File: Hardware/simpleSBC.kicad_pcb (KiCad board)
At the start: 6 copper layers, 49 x 55 mm, 124 parts, among them J1 Conn_02x07_Odd_Even, J2 Micro_SD_Card_Det, J3 Conn_01x06_Male, U1 STM32MP157FAD1, U2 LP2998, U3 MT41K256M16TW, X1 ASCO, Y1 32.786

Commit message: First Draft schematic (R2)
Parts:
- removed C39, C43, C44: 100u, Capacitor_SMD:C_1206_3216Metric
- removed C41: 4.7u, Capacitor_SMD:C_0402_1005Metric
- removed C42: 1u, Capacitor_SMD:C_0402_1005Metric
- removed C47: 100n, Capacitor_SMD:C_0402_1005Metric
- removed TP7, TP9: TestPoint, personal:PROBE_PAD_1206
- removed U2: LP2998, Package_SO:SOIC-8-1EP_3.9x4.9mm_P1.27mm_EP2.29x3mm_ThermalVias
- added C67: 1u, Capacitor_SMD:C_0402_1005Metric, F.Cu at (108.4, 42.9)
- added C68: 1u, Capacitor_SMD:C_0402_1005Metric, F.Cu at (108.4, 44.9)
- added C69: 1u, Capacitor_SMD:C_0402_1005Metric, F.Cu at (108.4, 46.9)
- added C70: 10u, Capacitor_SMD:C_0402_1005Metric, F.Cu at (108.4, 48.8)
- added C71: 10u, Capacitor_SMD:C_0402_1005Metric, F.Cu at (108.4, 50.8)
- added C72: 10u, Capacitor_SMD:C_0402_1005Metric, F.Cu at (111.3, 42.9)
- added C73: 10u, Capacitor_SMD:C_0402_1005Metric, F.Cu at (111.3, 44.9)
- added C74: 4.7u, Capacitor_SMD:C_0402_1005Metric, F.Cu at (111.3, 46.9)
- added C75: 1u, Capacitor_SMD:C_0402_1005Metric, F.Cu at (111.3, 48.8)
- added C76: 1u, Capacitor_SMD:C_0402_1005Metric, F.Cu at (111.3, 50.8)
- added J5: USB_A, Connector_USB:USB_A_Molex_67643_Horizontal, F.Cu at (147.8, 70.9)
- added J6: USB_A, Connector_USB:USB_A_Molex_67643_Horizontal, F.Cu at (127.0, 70.9)
- added U4: STPMIC1, SimpleSBC:WFQFN44L, F.Cu at (119.8, 103.0)
- U1: footprint personal:TFBGA257 -> SimpleSBC:TFBGA257
- moved TP6 41.8 mm to (134.5, 32.2)
- moved TP2 28.6 mm to (152.1, 48.2)
- moved TP4 26.1 mm to (127.0, 44.0)
- moved TP1 16.0 mm to (141.0, 47.2)
- moved TP5 15.9 mm to (120.5, 46.8)
- moved TP3 15.6 mm to (133.0, 47.8)
- moved TP8 13.4 mm to (166.0, 95.5)
- moved J2 13.3 mm to (139.8, 107.0), turned to 180 degrees
- moved R11 11.2 mm to (142.2, 98.7)
- moved R12 11.2 mm to (134.4, 98.7)
- moved R14 11.2 mm to (136.8, 98.7)
- moved R15 11.2 mm to (138.8, 98.7)
- moved R10 11.2 mm to (141.0, 98.7)
- moved R13 11.2 mm to (135.6, 98.7)
- moved J1 10.2 mm to (148.2, 107.6), turned to 90 degrees
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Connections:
- net /A0 renamed /Memory/A0
- net /A1 renamed /Memory/A1
- net /A10 renamed /Memory/A10
- net /A11 renamed /Memory/A11
- net /A12 renamed /Memory/A12
- net /A13 renamed /Memory/A13
- net /A14 renamed /Memory/A14
- net /A2 renamed /Memory/A2
- net /A3 renamed /Memory/A3
- net /A4 renamed /Memory/A4
- net /A5 renamed /Memory/A5
- net /A6 renamed /Memory/A6
- net /A7 renamed /Memory/A7
- net /A8 renamed /Memory/A8
- net /A9 renamed /Memory/A9
- net /BA0 renamed /Memory/BA0
- net /BA1 renamed /Memory/BA1
- net /BA2 renamed /Memory/BA2
- net /CKE renamed /Memory/CKE
- net /DDR_CK+ renamed /Memory/DDR_CK+
- net /DDR_CK- renamed /Memory/DDR_CK-
- net /DQ0 renamed /Memory/DQ0
- net /DQ1 renamed /Memory/DQ1
- net /DQ10 renamed /Memory/DQ10
- net /DQ11 renamed /Memory/DQ11
- net /DQ12 renamed /Memory/DQ12
- net /DQ13 renamed /Memory/DQ13
- net /DQ14 renamed /Memory/DQ14
- net /DQ15 renamed /Memory/DQ15
- net /DQ2 renamed /Memory/DQ2
- net /DQ3 renamed /Memory/DQ3
- net /DQ4 renamed /Memory/DQ4
- net /DQ5 renamed /Memory/DQ5
- net /DQ6 renamed /Memory/DQ6
- net /DQ7 renamed /Memory/DQ7
- net /DQ8 renamed /Memory/DQ8
- net /DQ9 renamed /Memory/DQ9
- net /LDM renamed /Memory/LDM
- net /LDQS+ renamed /Memory/LDQS+
- net /LDQS- renamed /Memory/LDQS-
- net /ODT renamed /Memory/ODT
- net /UDM renamed /Memory/UDM
- net /UDQS+ renamed /Memory/UDQS+
- net /UDQS- renamed /Memory/UDQS-
- net /~{CAS} renamed /Memory/~{CAS}
- net /~{CS} renamed /Memory/~{CS}
- net /~{RAS} renamed /Memory/~{RAS}
- net /~{RESET} renamed /Memory/~{RESET}
- net /~{WE} renamed /Memory/~{WE}
- J2 pad 1: /SDMMC_D2 -> /Memory/SDMMC_D2
- J2 pad 2: /SDMMC_D3 -> /Memory/SDMMC_D3
- J2 pad 3: /SDMMC_CMD -> /Memory/SDMMC_CMD
- J2 pad 5: /SDMMC_CLK -> /Memory/SDMMC_CLK
- J2 pad 7: /SDMMC_D0 -> /Memory/SDMMC_D0
- J2 pad 8: /SDMMC_D1 -> /Memory/SDMMC_D1
- R10 pad 1: /SDMMC_D0 -> /Memory/SDMMC_D0
- R11 pad 1: /SDMMC_D1 -> /Memory/SDMMC_D1
- R12 pad 1: /SDMMC_D2 -> /Memory/SDMMC_D2
- R13 pad 1: /SDMMC_D3 -> /Memory/SDMMC_D3
- R14 pad 1: /SDMMC_CMD -> /Memory/SDMMC_CMD
- R15 pad 1: /SDMMC_CLK -> /Memory/SDMMC_CLK
- U1 pad N3: unconnected-(U1-PadN3) -> /PA0_WAKEUP
- U1 pad V10: unconnected-(U1-PadV10) -> Net-(J5-D+)
- U1 pad V14: unconnected-(U1-PadV14) -> Net-(J6-D-)
- U1 pad W10: unconnected-(U1-PadW10) -> Net-(J5-D-)
- U1 pad W14: unconnected-(U1-PadW14) -> Net-(J6-D+)
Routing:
- net /SDMMC_D2: track 30.6 -> 0.00 mm, vias 2 -> 0
- net /Memory/SDMMC_D2: track 0.00 -> 30.6 mm, vias 0 -> 2
- net /SDMMC_CMD: track 30.0 -> 0.00 mm, vias 2 -> 0
- net /Memory/SDMMC_CMD: track 0.00 -> 30.0 mm, vias 0 -> 2
- net /SDMMC_CLK: track 29.1 -> 0.00 mm, vias 2 -> 0
- net /Memory/SDMMC_CLK: track 0.00 -> 29.1 mm, vias 0 -> 2
- net /SDMMC_D0: track 26.2 -> 0.00 mm, vias 2 -> 0
- net /Memory/SDMMC_D0: track 0.00 -> 26.2 mm, vias 0 -> 2
- net /IO2: track 13.2 -> 0.00 mm
- net /IO6: track 13.2 -> 0.00 mm
- net /IO3: track 12.4 -> 0.00 mm
- net /IO5: track 12.3 -> 0.00 mm
- net /IO4: track 11.9 -> 0.00 mm
- net /IO1: track 14.5 -> 3.30 mm
- net VTT_DDR: track 18.2 -> 9.38 mm, vias 7 -> 3
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- removed copper zone on F.Cu, net +1V2
- removed copper zone on F.Cu, net +1V35
- removed copper zone on F.Cu, net +3V3
- removed copper zone on F.Cu, net VTT_DDR
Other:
- outline, holes or cut-outs redrawn
- board text added: "Hans Gaensbauer and Tim Shepard"
- board text added: "SimpleSBC"
- board text removed: "Ap-Eval Designed by Hans Gaensbauer"

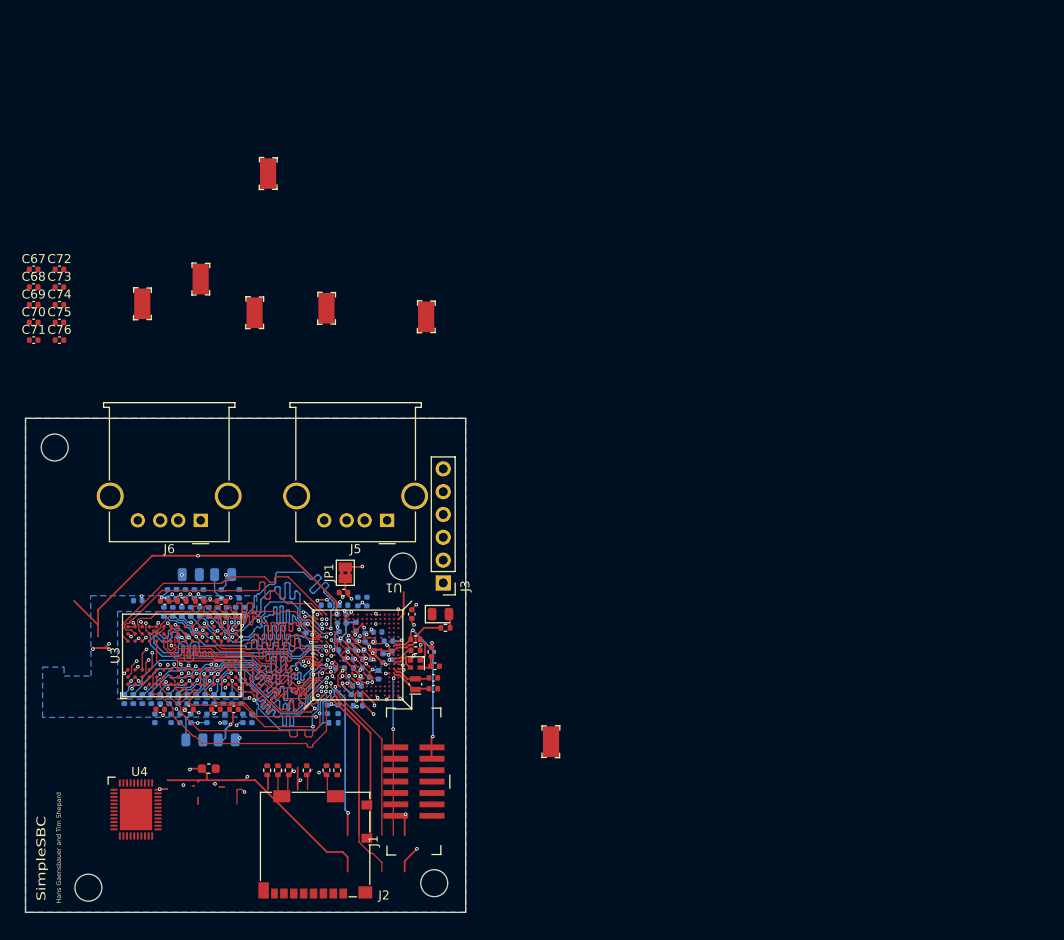
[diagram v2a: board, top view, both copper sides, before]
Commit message: Add Ethernet and USB power switching
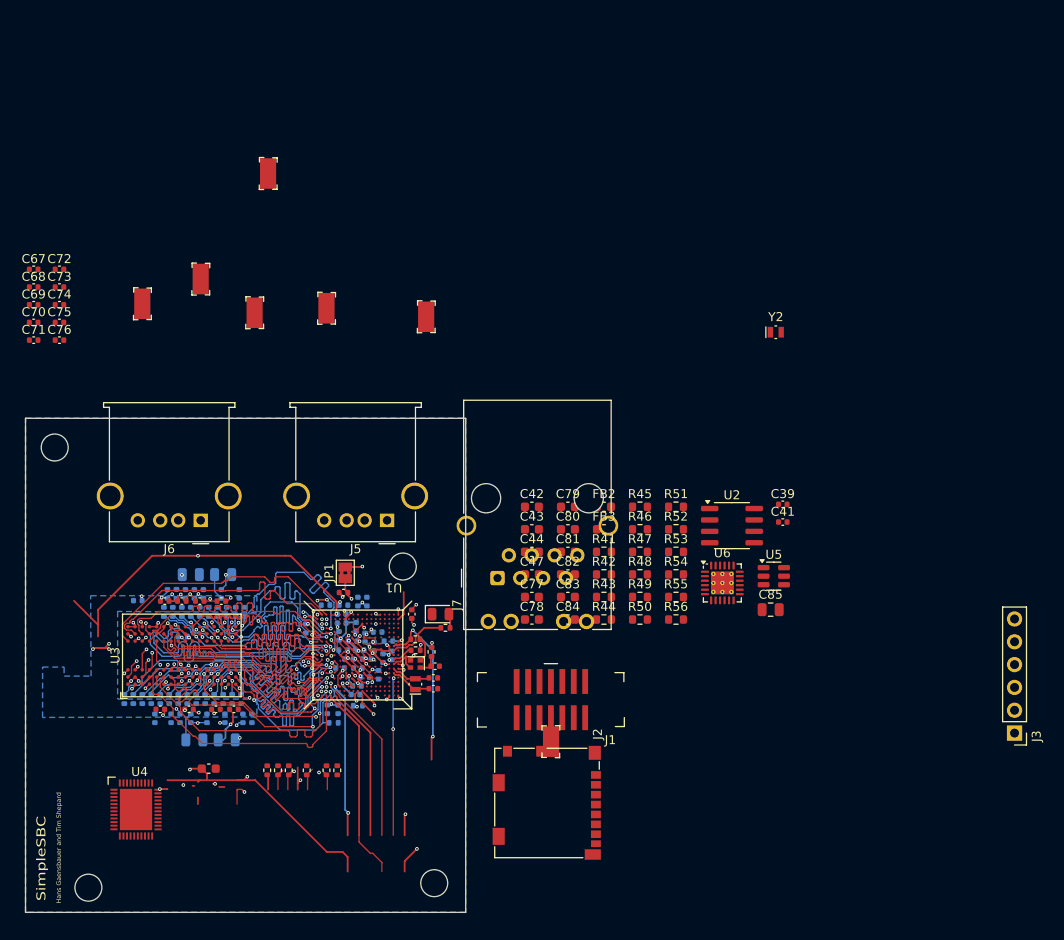
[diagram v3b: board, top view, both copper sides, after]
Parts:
- added C39: 47u, Capacitor_SMD:C_0402_1005Metric, F.Cu at (191.8, 69.1)
- added C41: 47u, Capacitor_SMD:C_0402_1005Metric, F.Cu at (191.8, 71.0)
- added C42: 30p, Capacitor_SMD:C_0603_1608Metric, F.Cu at (163.9, 69.3)
- added C43: 100n, Capacitor_SMD:C_0603_1608Metric, F.Cu at (163.9, 71.9)
- added C44: 30p, Capacitor_SMD:C_0603_1608Metric, F.Cu at (163.9, 74.4)
- added C47: 100n, Capacitor_SMD:C_0603_1608Metric, F.Cu at (163.9, 76.9)
- added C77: 1u, Capacitor_SMD:C_0603_1608Metric, F.Cu at (163.9, 79.4)
- added C78: 1u, Capacitor_SMD:C_0603_1608Metric, F.Cu at (163.9, 81.9)
- added C79: 1u, Capacitor_SMD:C_0603_1608Metric, F.Cu at (167.9, 69.3)
- added C80: 470p, Capacitor_SMD:C_0603_1608Metric, F.Cu at (167.9, 71.9)
- added C81: 100n, Capacitor_SMD:C_0603_1608Metric, F.Cu at (167.9, 74.4)
- added C82: 100n, Capacitor_SMD:C_0603_1608Metric, F.Cu at (167.9, 76.9)
- added C83: 100n, Capacitor_SMD:C_0603_1608Metric, F.Cu at (167.9, 79.4)
- added C84: 100n, Capacitor_SMD:C_0603_1608Metric, F.Cu at (167.9, 81.9)
- added C85: 10u, Capacitor_SMD:C_0805_2012Metric, F.Cu at (190.4, 80.8)
- added FB2: FerriteBead_Small, Inductor_SMD:L_0603_1608Metric, F.Cu at (171.9, 69.3)
- added FB3: FerriteBead_Small, Inductor_SMD:L_0603_1608Metric, F.Cu at (171.9, 71.9)
- added J7: RJ45_Wuerth_7499010121A, Connector_RJ:RJ45_Wuerth_7499010121A_Horizontal, F.Cu at (160.0, 77.3)
- added R41: 10k, Resistor_SMD:R_0603_1608Metric, F.Cu at (171.9, 74.4)
- added R42: 33, Resistor_SMD:R_0603_1608Metric, F.Cu at (171.9, 76.9)
- added R43: 33, Resistor_SMD:R_0603_1608Metric, F.Cu at (171.9, 79.4)
- added R44: 33, Resistor_SMD:R_0603_1608Metric, F.Cu at (171.9, 81.9)
- added R45: 270, Resistor_SMD:R_0603_1608Metric, F.Cu at (175.9, 69.3)
- added R46: 10k, Resistor_SMD:R_0603_1608Metric, F.Cu at (175.9, 71.9)
- added R47: 10k, Resistor_SMD:R_0603_1608Metric, F.Cu at (175.9, 74.4)
- added R48: 33, Resistor_SMD:R_0603_1608Metric, F.Cu at (175.9, 76.9)
- added R49: 10k, Resistor_SMD:R_0603_1608Metric, F.Cu at (175.9, 79.4)
- added R50: 270, Resistor_SMD:R_0603_1608Metric, F.Cu at (175.9, 81.9)
- added R51: 10k, Resistor_SMD:R_0603_1608Metric, F.Cu at (179.9, 69.3)
- added R52: 51, Resistor_SMD:R_0603_1608Metric, F.Cu at (179.9, 71.9)
- added R53: 51, Resistor_SMD:R_0603_1608Metric, F.Cu at (179.9, 74.4)
- added R54: 12.1k, Resistor_SMD:R_0603_1608Metric, F.Cu at (179.9, 76.9)
- added R55: 51, Resistor_SMD:R_0603_1608Metric, F.Cu at (179.9, 79.4)
- added R56: 51, Resistor_SMD:R_0603_1608Metric, F.Cu at (179.9, 81.9)
- added U2: STMPS2252MTR, Package_SO:SOIC-8_3.9x4.9mm_P1.27mm, F.Cu at (186.1, 71.5)
- added U5: USBLC6-4SC6, Package_TO_SOT_SMD:SOT-23-6, F.Cu at (190.8, 77.1)
- added U6: LAN8742A, Package_DFN_QFN:VQFN-24-1EP_4x4mm_P0.5mm_EP2.5x2.5mm_ThermalVias, F.Cu at (185.1, 77.8)
- added Y2: X53T-C20SSA-25.000MHz, Crystal:Crystal_SMD_MicroCrystal_CM9V-T1A-2Pin_1.6x1.0mm, F.Cu at (191.0, 49.9)
- moved J3 65.8 mm to (217.6, 94.5)
- moved J1 29.1 mm to (173.6, 93.3), turned to 180 degrees
- moved J2 26.2 mm to (165.6, 102.3), turned to -90 degrees
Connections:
- J5 pad 1: unconnected-(J5-VBUS-Pad1) -> Net-(J5-VBUS)
- J6 pad 1: unconnected-(J6-VBUS-Pad1) -> Net-(J6-VBUS)
- U1 pad R2: unconnected-(U1B-PG14-PadR2) -> /RMII_TXD_1
- U1 pad R3: unconnected-(U1B-PG13-PadR3) -> /RMII_TXD_0
- U1 pad T1: unconnected-(U1B-PA1-PadT1) -> /RMII_REF_CLK
- U1 pad T2: unconnected-(U1B-PC1-PadT2) -> /MDC
- U1 pad T3: unconnected-(U1B-PA2-PadT3) -> /MDIO
- U1 pad U3: unconnected-(U1B-PB11-PadU3) -> /RMII_TX_EN
- U1 pad V1: /IO1 -> /RMII_RX_D1
- U1 pad V2: unconnected-(U1B-PC4-PadV2) -> /RMII_RX_D0
- U1 pad W2: /IO2 -> /RMII_CRS_DV
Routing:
- net /RMII_RX_D1: track 0.00 -> 3.30 mm
- net /IO1: track 3.30 -> 0.00 mm

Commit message: First pass through ST Design Checklist
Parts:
- removed J3: Conn_01x06_Male, Connector_PinHeader_2.54mm:PinHeader_1x06_P2.54mm_Vertical
- added C86: 4.7u, Capacitor_SMD:C_0402_1005Metric, F.Cu at (180.7, 33.2)
- added FB1: FerriteBead_Small, Inductor_SMD:L_0603_1608Metric, F.Cu at (164.1, 37.9)
- added J4: Barrel_Jack_Switch, Connector_BarrelJack:BarrelJack_Wuerth_6941xx301002, F.Cu at (167.6, 18.5)
- added J8: Conn_01x03, Connector_PinHeader_2.54mm:PinHeader_1x03_P2.54mm_Vertical, F.Cu at (181.6, 18.9)
- added J9: Conn_01x06, Connector_PinHeader_2.54mm:PinHeader_1x06_P2.54mm_Vertical, F.Cu at (206.6, 74.1)
- added L1: 1u, Inductor_SMD:L_1008_2520Metric, F.Cu at (176.8, 18.4)
- added L2: 1u, Inductor_SMD:L_1008_2520Metric, F.Cu at (176.8, 22.2)
- added L3: 1u, Inductor_SMD:L_1008_2520Metric, F.Cu at (176.8, 25.9)
- added L4: 1u, Inductor_SMD:L_1008_2520Metric, F.Cu at (176.8, 29.7)
- added R57: 2.2k, Resistor_SMD:R_0402_1005Metric, F.Cu at (180.7, 29.2)
- added R58: 2.2k, Resistor_SMD:R_0402_1005Metric, F.Cu at (180.7, 31.2)
- added R9: 0, Resistor_SMD:R_0402_1005Metric, F.Cu at (180.7, 27.2)
- added TP10: TestPoint, TestPoint:TestPoint_Pad_D1.0mm, F.Cu at (175.9, 33.1)
- C42, C43, C44, C47, C77, C78, C79, C80, C81, C82, C83, C84: footprint Capacitor_SMD:C_0603_1608Metric -> Capacitor_SMD:C_0402_1005Metric
- J1: footprint personal:PinHeader_2x7_P1.27mm_SMD -> SimpleSBC:PinHeader_2x7_P1.27mm_SMD
- J2: value Micro_SD_Card_Det -> Micro_SD_Card_Det2
- R41, R42, R43, R44, R45, R46, R47, R48, R49, R50, R51, R52, R53, R54, R55, R56: footprint Resistor_SMD:R_0603_1608Metric -> Resistor_SMD:R_0402_1005Metric
- TP1, TP2, TP3, TP4, TP5, TP6: value TestPoint-SP -> TestPoint; footprint personal:PROBE_PAD_1206 -> TestPoint:TestPoint_Pad_D1.0mm
- TP8: footprint personal:PROBE_PAD_1206 -> TestPoint:TestPoint_Pad_D1.0mm
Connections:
- J2 pad 1: /Memory/SDMMC_D2 -> /SDMMC_D2
- J2 pad 2: /Memory/SDMMC_D3 -> /SDMMC_D3
- J2 pad 3: /Memory/SDMMC_CMD -> /SDMMC_CMD
- J2 pad 5: /Memory/SDMMC_CLK -> /SDMMC_CLK
- J2 pad 7: /Memory/SDMMC_D0 -> /SDMMC_D0
- J2 pad 8: /Memory/SDMMC_D1 -> /SDMMC_D1
- R10 pad 1: /Memory/SDMMC_D0 -> /SDMMC_D0
- R11 pad 1: /Memory/SDMMC_D1 -> /SDMMC_D1
- R12 pad 1: /Memory/SDMMC_D2 -> /SDMMC_D2
- R13 pad 1: /Memory/SDMMC_D3 -> /SDMMC_D3
- R14 pad 1: /Memory/SDMMC_CMD -> /SDMMC_CMD
- R15 pad 1: /Memory/SDMMC_CLK -> /SDMMC_CLK
- TP1 pad 1: +3V3 -> +1V2
- TP2 pad 1: GND -> +1V35
- TP3 pad 1: +1V2 -> +3V3
- TP4 pad 1: GND -> +3.3VP
- TP5 pad 1: +1V35 -> VREF_DDR
- TP6 pad 1: GND -> VTT_DDR
- U4 pad 20: unconnected-(U4-LDO5OUT-Pad20) -> Net-(U4-LDO5OUT)
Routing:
- net (no net): track 0.00 -> 79.8 mm
- net /Memory/SDMMC_D2: track 30.6 -> 0.00 mm, vias 2 -> 0
- net /Memory/SDMMC_CMD: track 30.0 -> 0.00 mm, vias 2 -> 0
- net /SDMMC_CMD: track 0.00 -> 29.8 mm, vias 0 -> 2
- net /Memory/SDMMC_CLK: track 29.1 -> 0.00 mm, vias 2 -> 0
- net /Memory/SDMMC_D0: track 26.2 -> 0.00 mm, vias 2 -> 0
- net /SDMMC_CLK: track 0.00 -> 2.55 mm, vias 0 -> 2
- net /Memory/SDMMC_D3: track 2.33 -> 0.00 mm
- net /SDMMC_D3: track 28.9 -> 31.3 mm
- net /SDMMC_D0: track 0.00 -> 2.06 mm, vias 0 -> 2
- net /SDMMC_D2: track 0.00 -> 1.68 mm, vias 0 -> 2

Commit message: First Pass for Floorplanning
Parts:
- removed C45: 1u, Capacitor_SMD:C_0402_1005Metric
- removed FB2: FerriteBead_Small, Inductor_SMD:L_0603_1608Metric
- removed Y2: X53T-C20SSA-25.000MHz, Crystal:Crystal_SMD_MicroCrystal_CM9V-T1A-2Pin_1.6x1.0mm
- added C87: 10u, Capacitor_SMD:C_0603_1608Metric, F.Cu at (127.2, 111.5)
- added C88: 4.7u, Capacitor_SMD:C_0402_1005Metric, F.Cu at (132.2, 99.0)
- added C89: 10u, Capacitor_SMD:C_0603_1608Metric, F.Cu at (136.9, 98.0)
- added C90: 22u, Capacitor_SMD:C_0805_2012Metric, F.Cu at (124.9, 101.8)
- added C91: 22u, Capacitor_SMD:C_0805_2012Metric, F.Cu at (123.7, 106.5)
- added C92: 22u, Capacitor_SMD:C_0805_2012Metric, F.Cu at (140.8, 104.2)
- added C93: 22u, Capacitor_SMD:C_0805_2012Metric, F.Cu at (139.2, 108.8)
- added C94: 10u, Capacitor_SMD:C_0603_1608Metric, F.Cu at (128.7, 111.5)
- added C95: 4.7u, Capacitor_SMD:C_0402_1005Metric, F.Cu at (133.9, 111.0)
- added C96: 4.7u, Capacitor_SMD:C_0402_1005Metric, F.Cu at (134.9, 108.0)
- added C97: 10n, Capacitor_SMD:C_0402_1005Metric, F.Cu at (166.5, 107.2)
- added D2: LED_Small, LED_SMD:LED_0805_2012Metric, F.Cu at (153.8, 78.5)
- added R59: 0, Resistor_SMD:R_0402_1005Metric, F.Cu at (135.9, 99.8)
- added R60: 10k, Resistor_SMD:R_0402_1005Metric, F.Cu at (157.2, 107.2)
- added R61: 330, Resistor_SMD:R_0402_1005Metric, F.Cu at (154.2, 77.0)
- added R62: 3k, Resistor_SMD:R_0402_1005Metric, F.Cu at (146.0, 78.2)
- added R63: 10k, Resistor_SMD:R_0402_1005Metric, F.Cu at (167.5, 107.2)
- C40: value 100n -> 10n
- C51, C77, C78, C81, C82, R10, R11, R12, R13, R14, R15, R45, R47, R50, TP1, TP10, TP2, TP3, TP4, TP5, TP6: moved to B.Cu
- C69, C76: value 1u -> 4.7u
- C70, C71, C72, C73: footprint Capacitor_SMD:C_0402_1005Metric -> Capacitor_SMD:C_0603_1608Metric
- R8: value 1k -> 470
- moved J8 103.7 mm to (110.5, 94.3), turned to 180 degrees
- moved J4 98.2 mm to (113.4, 100.4)
- moved L2 98.2 mm to (126.9, 106.8), turned to 180 degrees
- moved L1 97.1 mm to (127.4, 102.0), turned to 90 degrees
- moved R57 92.3 mm to (113.5, 92.5)
- moved R58 92.3 mm to (113.5, 94.5)
- moved TP10 91.8 mm to (131.2, 113.2), turned to 180 degrees
- moved C86 91.3 mm to (132.9, 111.0), turned to 90 degrees
- moved L3 85.8 mm to (137.7, 102.2)
- moved R9 85.6 mm to (134.2, 99.0), turned to 90 degrees
- moved L4 85.3 mm to (139.2, 106.2)
- moved C39 82.6 mm to (109.8, 79.0), turned to 90 degrees
- moved C41 81.4 mm to (110.8, 79.0), turned to 90 degrees
- moved C67 71.7 mm to (134.9, 109.5)
- moved TP4 71.6 mm to (148.8, 112.2)
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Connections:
- net /Power/I2C4_SCL renamed /I2C4_SCL
- net /Power/I2C4_SDA renamed /I2C4_SDA
- net /Power/NRST renamed /Power/~{RST}
- C49 pad 1: Net-(JP1-A) -> VDD_USB
- C51 pad 1: +3V3 -> +3.3VP
- C76 pad 2: VTT_DDR -> Net-(U4-LDO2OUT)
- C77 pad 1: Net-(J7-RCT) -> +3V3
- C78 pad 1: Net-(J7-RCT) -> +3V3
- C81 pad 1: Net-(J7-RCT) -> +3V3
- C82 pad 1: Net-(J7-RCT) -> +3V3
- J2 pad 4: +3V3 -> +3.3VP
- J7 pad 2: Net-(J7-RCT) -> +3V3
- J7 pad 5: Net-(J7-RCT) -> +3V3
- J7 pad SH: Net-(FB2-Pad1) -> unconnected-(J7-PadSH)_1
- U1 pad 1A7: Net-(U1A-VDD1V2_DSI_PHY) -> unconnected-(U1A-VDD1V2_DSI_REG-Pad1A7)
- U1 pad 1B7: Net-(U1A-VDD1V2_DSI_PHY) -> unconnected-(U1A-VDD1V2_DSI_PHY-Pad1B7)
- U1 pad 1H7: Net-(JP1-A) -> VDD_USB
- U1 pad 1J8: unconnected-(U1C-USB_RREF-Pad1J8) -> Net-(U1C-USB_RREF)
- U1 pad B18: /Memory/LDQS+ -> /Memory/UDQS-
- U1 pad B19: /Memory/LDQS- -> /Memory/UDQS+
- U1 pad C17: /Memory/LDM -> /Memory/UDM
- U1 pad G3: unconnected-(U1B-PC13-PadG3) -> /RTC_OUT1
- U1 pad L1: unconnected-(U1B-PA14-PadL1) -> Net-(U1B-PA14)
- U1 pad U13: unconnected-(U1B-PD13-PadU13) -> Net-(JP3-A)
- U1 pad U14: unconnected-(U1B-PD12-PadU14) -> Net-(JP2-A)
- U1 pad U18: /Memory/UDQS+ -> /Memory/LDQS-
- U1 pad V18: /Memory/UDM -> /Memory/LDM
- U1 pad V19: /Memory/UDQS- -> /Memory/LDQS+
- U2 pad 5: unconnected-(U2-~{OC2}-Pad5) -> /USB_~{OC2}
- U2 pad 8: unconnected-(U2-~{OC1}-Pad8) -> /USB_~{OC1}
- U4 pad 18: unconnected-(U4-LDO2OUT-Pad18) -> Net-(U4-LDO2OUT)
- U4 pad 2: /Power/PMIC_WAKEUP -> /RTC_OUT1
- U4 pad 21: unconnected-(U4-LDO6OUT-Pad21) -> Net-(U4-LDO6OUT)
- U4 pad 23: unconnected-(U4-LDO1OUT-Pad23) -> Net-(U4-LDO1OUT)
- U4 pad 33: +5V -> Net-(U4-VLXBST)
- U4 pad 39: unconnected-(U4-LDO4OUT-Pad39) -> VDD_USB
- U4 pad 43: /Power/PA0_WAKEUP -> /PA0_WAKEUP
- U4 pad 44: /Power/PWR_ON -> /PWR_ON
- U6 pad 15: /~{RST} -> unconnected-(U6-~{RST}-Pad15)
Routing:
- net (no net): track 79.8 -> 2.35 mm, vias 0 -> 1
- net +3V3: track 53.3 -> 20.0 mm, vias 13 -> 10
- net /SDMMC_D3: track 31.3 -> 5.85 mm, vias 2 -> 1
- net /SDMMC_CMD: track 29.8 -> 5.59 mm, vias 2 -> 1
- net /SDMMC_D1: track 24.6 -> 4.03 mm, vias 2 -> 1
- net /UART4_TX: track 25.1 -> 7.00 mm, vias 2 -> 1
- net /SWCLK: track 22.1 -> 4.65 mm
- net /SWDIO: track 17.1 -> 1.72 mm, vias 2 -> 1
- net VREF_DDR: track 61.7 -> 46.4 mm
- net /NRST: track 17.5 -> 5.71 mm
- net /SWO: track 17.1 -> 5.72 mm
- net /JTDI: track 18.2 -> 7.44 mm
- net /SDMMC_CLK: track 2.55 -> 6.20 mm, vias 2 -> 1
- net /UART4_RX: track 35.7 -> 32.5 mm, vias 2 -> 1
- net Net-(U1A-VDD1V2_DSI_PHY): track 2.35 -> 0.00 mm, vias 1 -> 0
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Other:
- board size 49 x 55 mm -> 66 x 56 mm
